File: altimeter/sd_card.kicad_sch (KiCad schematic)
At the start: 7 parts, among them J5 Micro_SD_Card

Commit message: add footprints to all components but e-match connectors
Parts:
- J5: footprint canhw:microSD_Molex_WM6698CT-ND -> canhw_footprints:microSD_Molex_WM6698CT-ND
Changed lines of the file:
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@@
 			)
 		)
-		(property "Footprint" "canhw:microSD_Molex_WM6698CT-ND"
+		(property "Footprint" "canhw_footprints:microSD_Molex_WM6698CT-ND"
 			(at 222.504 96.52 0)
 			(effects

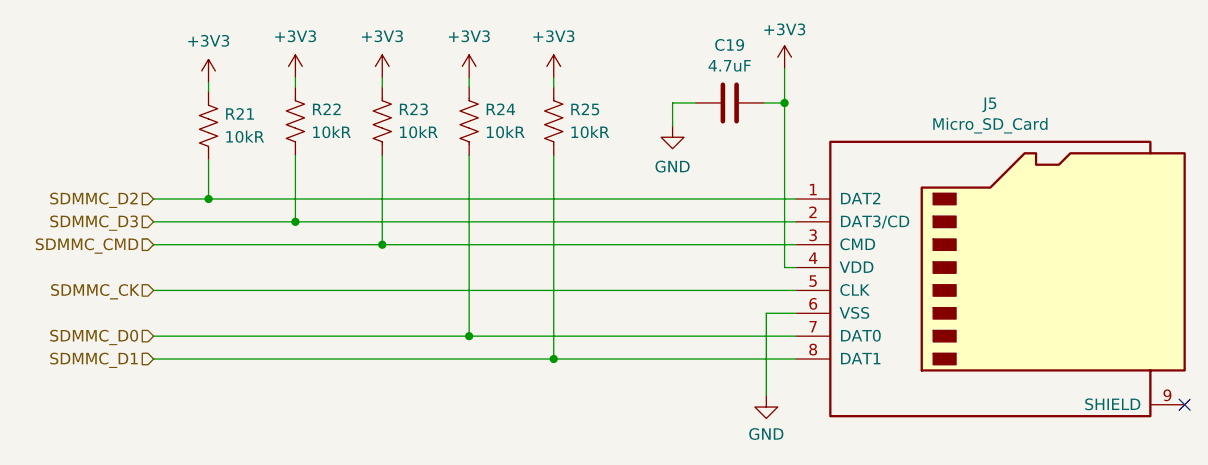
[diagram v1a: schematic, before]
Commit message: renumber all refdes
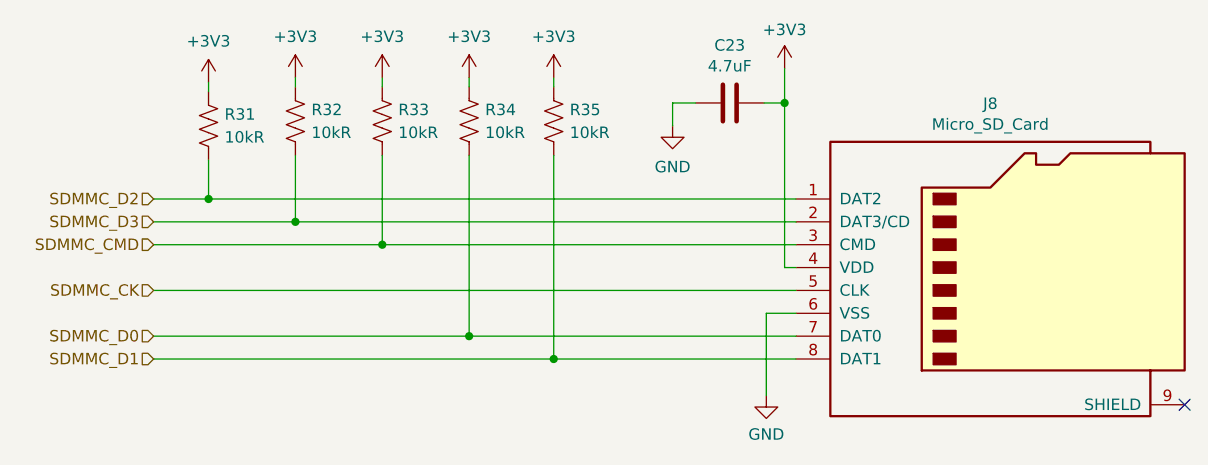
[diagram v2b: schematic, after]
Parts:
- renumbered C19 to C23, J5 to J8, R21 to R31, R22 to R32, R23 to R33, R24 to R34, R25 to R35
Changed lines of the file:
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@@
 		(dnp no)
 		(fields_autoplaced yes)
-		(property "Reference" "R23"
+		(property "Reference" "R33"
 			(at 126.238 86.614 0)
 			(effects
@@
 			(project "altimeter"
 				(path "/d279ec14-0cf9-4295-bb74-26f70799167d/bb0bce4a-66e8-4d50-ad75-3628c6e07bf2/e008a181-ebf7-4a64-a582-05387fd5f501"
-					(reference "R23")
+					(reference "R33")
 					(unit 1)
 				)
@@
 		(dnp no)
 		(fields_autoplaced yes)
-		(property "Reference" "#PWR050"
+		(property "Reference" "#PWR077"
 			(at 114.808 86.868 0)
 			(effects
@@
 			(project "altimeter"
 				(path "/d279ec14-0cf9-4295-bb74-26f70799167d/bb0bce4a-66e8-4d50-ad75-3628c6e07bf2/e008a181-ebf7-4a64-a582-05387fd5f501"
-					(reference "#PWR050")
+					(reference "#PWR077")
 					(unit 1)
 				)
@@
 		(dnp no)
 		(fields_autoplaced yes)
-		(property "Reference" "#PWR052"
+		(property "Reference" "#PWR079"
 			(at 134.112 86.868 0)
 			(effects
@@
 			(project "altimeter"
 				(path "/d279ec14-0cf9-4295-bb74-26f70799167d/bb0bce4a-66e8-4d50-ad75-3628c6e07bf2/e008a181-ebf7-4a64-a582-05387fd5f501"
-					(reference "#PWR052")
+					(reference "#PWR079")
 					(unit 1)
 				)
@@
 		(dnp no)
 		(fields_autoplaced yes)
-		(property "Reference" "#PWR051"
+		(property "Reference" "#PWR078"
 			(at 124.46 86.868 0)
 			(effects
@@
 			(project "altimeter"
 				(path "/d279ec14-0cf9-4295-bb74-26f70799167d/bb0bce4a-66e8-4d50-ad75-3628c6e07bf2/e008a181-ebf7-4a64-a582-05387fd5f501"
-					(reference "#PWR051")
+					(reference "#PWR078")
 					(unit 1)
 				)
@@
 		(dnp no)
 		(fields_autoplaced yes)
-		(property "Reference" "#PWR053"
+		(property "Reference" "#PWR080"
 			(at 143.51 86.868 0)
 			(effects
@@
 			(project "altimeter"
 				(path "/d279ec14-0cf9-4295-bb74-26f70799167d/bb0bce4a-66e8-4d50-ad75-3628c6e07bf2/e008a181-ebf7-4a64-a582-05387fd5f501"
-					(reference "#PWR053")
+					(reference "#PWR080")
 					(unit 1)
 				)
@@
 		(dnp no)
 		(fields_autoplaced yes)
-		(property "Reference" "R25"
+		(property "Reference" "R35"
 			(at 145.288 86.614 0)
 			(effects
@@
 			(project "altimeter"
 				(path "/d279ec14-0cf9-4295-bb74-26f70799167d/bb0bce4a-66e8-4d50-ad75-3628c6e07bf2/e008a181-ebf7-4a64-a582-05387fd5f501"
-					(reference "R25")
+					(reference "R35")
 					(unit 1)
 				)
@@
 		(on_board yes)
 		(dnp no)
-		(property "Reference" "C19"
+		(property "Reference" "C23"
 			(at 163.068 79.4512 90)
 			(effects
@@
 			(project "altimeter"
 				(path "/d279ec14-0cf9-4295-bb74-26f70799167d/bb0bce4a-66e8-4d50-ad75-3628c6e07bf2/e008a181-ebf7-4a64-a582-05387fd5f501"
-					(reference "C19")
+					(reference "C23")
 					(unit 1)
 				)
@@
 		(dnp no)
 		(fields_autoplaced yes)
-		(property "Reference" "#PWR049"
+		(property "Reference" "#PWR076"
 			(at 105.156 87.376 0)
 			(effects
@@
 			(project "altimeter"
 				(path "/d279ec14-0cf9-4295-bb74-26f70799167d/bb0bce4a-66e8-4d50-ad75-3628c6e07bf2/e008a181-ebf7-4a64-a582-05387fd5f501"
-					(reference "#PWR049")
+					(reference "#PWR076")
 					(unit 1)
 				)
@@
 		(dnp no)
 		(fields_autoplaced yes)
-		(property "Reference" "R21"
+		(property "Reference" "R31"
 			(at 106.934 87.122 0)
 			(effects
@@
 			(project "altimeter"
 				(path "/d279ec14-0cf9-4295-bb74-26f70799167d/bb0bce4a-66e8-4d50-ad75-3628c6e07bf2/e008a181-ebf7-4a64-a582-05387fd5f501"
-					(reference "R21")
+					(reference "R31")
 					(unit 1)
 				)
@@
 		(dnp no)
 		(fields_autoplaced yes)
-		(property "Reference" "R22"
+		(property "Reference" "R32"
 			(at 116.586 86.614 0)
 			(effects
@@
 			(project "altimeter"
 				(path "/d279ec14-0cf9-4295-bb74-26f70799167d/bb0bce4a-66e8-4d50-ad75-3628c6e07bf2/e008a181-ebf7-4a64-a582-05387fd5f501"
-					(reference "R22")
+					(reference "R32")
 					(unit 1)
 				)
@@
 		(dnp no)
 		(fields_autoplaced yes)
-		(property "Reference" "#PWR055"
+		(property "Reference" "#PWR082"
 			(at 167.132 124.714 0)
 			(effects
@@
 			(project "altimeter"
 				(path "/d279ec14-0cf9-4295-bb74-26f70799167d/bb0bce4a-66e8-4d50-ad75-3628c6e07bf2/e008a181-ebf7-4a64-a582-05387fd5f501"
-					(reference "#PWR055")
+					(reference "#PWR082")
 					(unit 1)
 				)
@@
 		(dnp no)
 		(fields_autoplaced yes)
-		(property "Reference" "#PWR056"
+		(property "Reference" "#PWR083"
 			(at 169.164 85.852 0)
 			(effects
@@
 			(project "altimeter"
 				(path "/d279ec14-0cf9-4295-bb74-26f70799167d/bb0bce4a-66e8-4d50-ad75-3628c6e07bf2/e008a181-ebf7-4a64-a582-05387fd5f501"
-					(reference "#PWR056")
+					(reference "#PWR083")
 					(unit 1)
 				)
@@
 		(dnp no)
 		(fields_autoplaced yes)
-		(property "Reference" "R24"
+		(property "Reference" "R34"
 			(at 135.89 86.614 0)
 			(effects
@@
 			(project "altimeter"
 				(path "/d279ec14-0cf9-4295-bb74-26f70799167d/bb0bce4a-66e8-4d50-ad75-3628c6e07bf2/e008a181-ebf7-4a64-a582-05387fd5f501"
-					(reference "R24")
+					(reference "R34")
 					(unit 1)
 				)
@@
 		(on_board yes)
 		(dnp no)
-		(property "Reference" "J5"
+		(property "Reference" "J8"
 			(at 192.024 85.9282 0)
 			(effects
@@
 			(project "altimeter"
 				(path "/d279ec14-0cf9-4295-bb74-26f70799167d/bb0bce4a-66e8-4d50-ad75-3628c6e07bf2/e008a181-ebf7-4a64-a582-05387fd5f501"
-					(reference "J5")
+					(reference "J8")
 					(unit 1)
 				)
@@
 		(dnp no)
 		(fields_autoplaced yes)
-		(property "Reference" "#PWR054"
+		(property "Reference" "#PWR081"
 			(at 156.718 94.742 0)
 			(effects
@@
 			(project "altimeter"
 				(path "/d279ec14-0cf9-4295-bb74-26f70799167d/bb0bce4a-66e8-4d50-ad75-3628c6e07bf2/e008a181-ebf7-4a64-a582-05387fd5f501"
-					(reference "#PWR054")
-					(unit 1)
-				)
+					(reference "#PWR081")
+					(unit 1)
+				)

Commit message: address buck current backdrive, add pyro current limiting resistors, mag switch and fuses, voltage sensing, battery charge current sensing
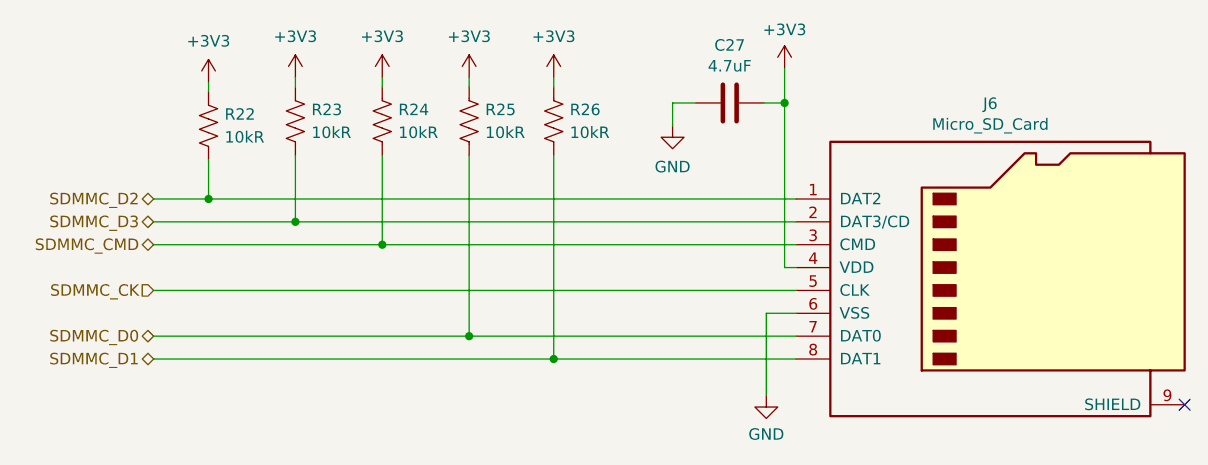
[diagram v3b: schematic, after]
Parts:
- renumbered C23 to C27, J8 to J6, R31 to R22, R32 to R23, R33 to R24, R34 to R25, R35 to R26
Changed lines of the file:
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@@
 	)
 	(hierarchical_label "SDMMC_D2"
-		(shape input)
+		(shape bidirectional)
 		(at 99.06 96.52 180)
 		(fields_autoplaced yes)
@@
 	)
 	(hierarchical_label "SDMMC_D0"
-		(shape input)
+		(shape bidirectional)
 		(at 99.06 111.76 180)
 		(fields_autoplaced yes)
@@
 	)
 	(hierarchical_label "SDMMC_D1"
-		(shape input)
+		(shape bidirectional)
 		(at 99.06 114.3 180)
 		(fields_autoplaced yes)
@@
 	)
 	(hierarchical_label "SDMMC_D3"
-		(shape input)
+		(shape bidirectional)
 		(at 99.06 99.06 180)
 		(fields_autoplaced yes)
@@
 	)
 	(hierarchical_label "SDMMC_CMD"
-		(shape input)
+		(shape bidirectional)
 		(at 99.06 101.6 180)
 		(fields_autoplaced yes)
@@
 		(dnp no)
 		(fields_autoplaced yes)
-		(property "Reference" "R33"
+		(property "Reference" "R24"
 			(at 126.238 86.614 0)
 			(effects
@@
 			(project "altimeter"
 				(path "/d279ec14-0cf9-4295-bb74-26f70799167d/bb0bce4a-66e8-4d50-ad75-3628c6e07bf2/e008a181-ebf7-4a64-a582-05387fd5f501"
-					(reference "R33")
+					(reference "R24")
 					(unit 1)
 				)
@@
 		(dnp no)
 		(fields_autoplaced yes)
-		(property "Reference" "#PWR077"
+		(property "Reference" "#PWR063"
 			(at 114.808 86.868 0)
 			(effects
@@
 			(project "altimeter"
 				(path "/d279ec14-0cf9-4295-bb74-26f70799167d/bb0bce4a-66e8-4d50-ad75-3628c6e07bf2/e008a181-ebf7-4a64-a582-05387fd5f501"
-					(reference "#PWR077")
+					(reference "#PWR063")
 					(unit 1)
 				)
@@
 		(dnp no)
 		(fields_autoplaced yes)
-		(property "Reference" "#PWR079"
+		(property "Reference" "#PWR065"
 			(at 134.112 86.868 0)
 			(effects
@@
 			(project "altimeter"
 				(path "/d279ec14-0cf9-4295-bb74-26f70799167d/bb0bce4a-66e8-4d50-ad75-3628c6e07bf2/e008a181-ebf7-4a64-a582-05387fd5f501"
-					(reference "#PWR079")
+					(reference "#PWR065")
 					(unit 1)
 				)
@@
 		(dnp no)
 		(fields_autoplaced yes)
-		(property "Reference" "#PWR078"
+		(property "Reference" "#PWR064"
 			(at 124.46 86.868 0)
 			(effects
@@
 			(project "altimeter"
 				(path "/d279ec14-0cf9-4295-bb74-26f70799167d/bb0bce4a-66e8-4d50-ad75-3628c6e07bf2/e008a181-ebf7-4a64-a582-05387fd5f501"
-					(reference "#PWR078")
+					(reference "#PWR064")
 					(unit 1)
 				)
@@
 		(dnp no)
 		(fields_autoplaced yes)
-		(property "Reference" "#PWR080"
+		(property "Reference" "#PWR066"
 			(at 143.51 86.868 0)
 			(effects
@@
 			(project "altimeter"
 				(path "/d279ec14-0cf9-4295-bb74-26f70799167d/bb0bce4a-66e8-4d50-ad75-3628c6e07bf2/e008a181-ebf7-4a64-a582-05387fd5f501"
-					(reference "#PWR080")
+					(reference "#PWR066")
 					(unit 1)
 				)
@@
 		(dnp no)
 		(fields_autoplaced yes)
-		(property "Reference" "R35"
+		(property "Reference" "R26"
 			(at 145.288 86.614 0)
 			(effects
@@
 			(project "altimeter"
 				(path "/d279ec14-0cf9-4295-bb74-26f70799167d/bb0bce4a-66e8-4d50-ad75-3628c6e07bf2/e008a181-ebf7-4a64-a582-05387fd5f501"
-					(reference "R35")
+					(reference "R26")
 					(unit 1)
 				)
@@
 		(on_board yes)
 		(dnp no)
-		(property "Reference" "C23"
+		(property "Reference" "C27"
 			(at 163.068 79.4512 90)
 			(effects
@@
 			(project "altimeter"
 				(path "/d279ec14-0cf9-4295-bb74-26f70799167d/bb0bce4a-66e8-4d50-ad75-3628c6e07bf2/e008a181-ebf7-4a64-a582-05387fd5f501"
-					(reference "C23")
+					(reference "C27")
 					(unit 1)
 				)
@@
 		(dnp no)
 		(fields_autoplaced yes)
-		(property "Reference" "#PWR076"
+		(property "Reference" "#PWR062"
 			(at 105.156 87.376 0)
 			(effects
@@
 			(project "altimeter"
 				(path "/d279ec14-0cf9-4295-bb74-26f70799167d/bb0bce4a-66e8-4d50-ad75-3628c6e07bf2/e008a181-ebf7-4a64-a582-05387fd5f501"
-					(reference "#PWR076")
+					(reference "#PWR062")
 					(unit 1)
 				)
@@
 		(dnp no)
 		(fields_autoplaced yes)
-		(property "Reference" "R31"
+		(property "Reference" "R22"
 			(at 106.934 87.122 0)
 			(effects
@@
 			(project "altimeter"
 				(path "/d279ec14-0cf9-4295-bb74-26f70799167d/bb0bce4a-66e8-4d50-ad75-3628c6e07bf2/e008a181-ebf7-4a64-a582-05387fd5f501"
-					(reference "R31")
+					(reference "R22")
 					(unit 1)
 				)
@@
 		(dnp no)
 		(fields_autoplaced yes)
-		(property "Reference" "R32"
+		(property "Reference" "R23"
 			(at 116.586 86.614 0)
 			(effects
@@
 			(project "altimeter"
 				(path "/d279ec14-0cf9-4295-bb74-26f70799167d/bb0bce4a-66e8-4d50-ad75-3628c6e07bf2/e008a181-ebf7-4a64-a582-05387fd5f501"
-					(reference "R32")
+					(reference "R23")
 					(unit 1)
 				)
@@
 		(dnp no)
 		(fields_autoplaced yes)
-		(property "Reference" "#PWR082"
+		(property "Reference" "#PWR068"
 			(at 167.132 124.714 0)
 			(effects
@@
 			(project "altimeter"
 				(path "/d279ec14-0cf9-4295-bb74-26f70799167d/bb0bce4a-66e8-4d50-ad75-3628c6e07bf2/e008a181-ebf7-4a64-a582-05387fd5f501"
-					(reference "#PWR082")
+					(reference "#PWR068")
 					(unit 1)
 				)
@@
 		(dnp no)
 		(fields_autoplaced yes)
-		(property "Reference" "#PWR083"
+		(property "Reference" "#PWR069"
 			(at 169.164 85.852 0)
 			(effects
@@
 			(project "altimeter"
 				(path "/d279ec14-0cf9-4295-bb74-26f70799167d/bb0bce4a-66e8-4d50-ad75-3628c6e07bf2/e008a181-ebf7-4a64-a582-05387fd5f501"
-					(reference "#PWR083")
+					(reference "#PWR069")
 					(unit 1)
 				)
@@
 		(dnp no)
 		(fields_autoplaced yes)
-		(property "Reference" "R34"
+		(property "Reference" "R25"
 			(at 135.89 86.614 0)
 			(effects
@@
 			(project "altimeter"
 				(path "/d279ec14-0cf9-4295-bb74-26f70799167d/bb0bce4a-66e8-4d50-ad75-3628c6e07bf2/e008a181-ebf7-4a64-a582-05387fd5f501"
-					(reference "R34")
+					(reference "R25")
 					(unit 1)
 				)
@@
 		(on_board yes)
 		(dnp no)
-		(property "Reference" "J8"
+		(property "Reference" "J6"
 			(at 192.024 85.9282 0)
 			(effects
@@
 			(project "altimeter"
 				(path "/d279ec14-0cf9-4295-bb74-26f70799167d/bb0bce4a-66e8-4d50-ad75-3628c6e07bf2/e008a181-ebf7-4a64-a582-05387fd5f501"
-					(reference "J8")
+					(reference "J6")
 					(unit 1)
 				)
@@
 		(dnp no)
 		(fields_autoplaced yes)
-		(property "Reference" "#PWR081"
+		(property "Reference" "#PWR067"
 			(at 156.718 94.742 0)
 			(effects
@@
 			(project "altimeter"
 				(path "/d279ec14-0cf9-4295-bb74-26f70799167d/bb0bce4a-66e8-4d50-ad75-3628c6e07bf2/e008a181-ebf7-4a64-a582-05387fd5f501"
-					(reference "#PWR081")
-					(unit 1)
-				)
+					(reference "#PWR067")
+					(unit 1)
+				)

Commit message: source/size buzzer, fuses, voltage divider resistors, add battery and +pyro voltage sense, gps connector and mcp2562, and capacitor to prevent brownout on 3v3
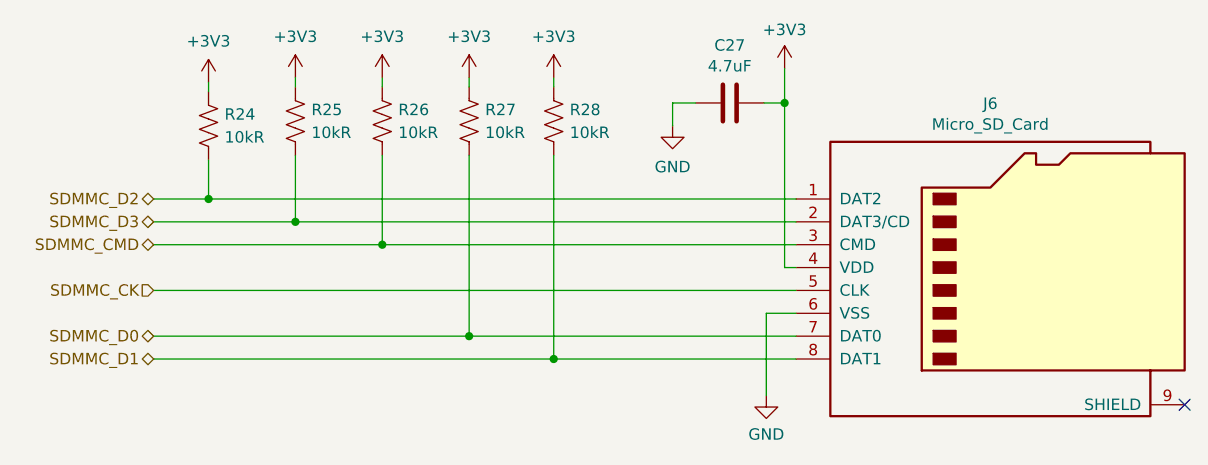
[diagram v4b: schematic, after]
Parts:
- renumbered R22 to R24, R23 to R25, R24 to R26, R25 to R27, R26 to R28
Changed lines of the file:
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@@
 		(dnp no)
 		(fields_autoplaced yes)
-		(property "Reference" "R24"
+		(property "Reference" "R26"
 			(at 126.238 86.614 0)
 			(effects
@@
 			(project "altimeter"
 				(path "/d279ec14-0cf9-4295-bb74-26f70799167d/bb0bce4a-66e8-4d50-ad75-3628c6e07bf2/e008a181-ebf7-4a64-a582-05387fd5f501"
-					(reference "R24")
+					(reference "R26")
 					(unit 1)
 				)
@@
 		(dnp no)
 		(fields_autoplaced yes)
-		(property "Reference" "#PWR063"
+		(property "Reference" "#PWR064"
 			(at 114.808 86.868 0)
 			(effects
@@
 			(project "altimeter"
 				(path "/d279ec14-0cf9-4295-bb74-26f70799167d/bb0bce4a-66e8-4d50-ad75-3628c6e07bf2/e008a181-ebf7-4a64-a582-05387fd5f501"
-					(reference "#PWR063")
+					(reference "#PWR064")
 					(unit 1)
 				)
@@
 		(dnp no)
 		(fields_autoplaced yes)
-		(property "Reference" "#PWR065"
+		(property "Reference" "#PWR066"
 			(at 134.112 86.868 0)
 			(effects
@@
 			(project "altimeter"
 				(path "/d279ec14-0cf9-4295-bb74-26f70799167d/bb0bce4a-66e8-4d50-ad75-3628c6e07bf2/e008a181-ebf7-4a64-a582-05387fd5f501"
-					(reference "#PWR065")
+					(reference "#PWR066")
 					(unit 1)
 				)
@@
 		(dnp no)
 		(fields_autoplaced yes)
-		(property "Reference" "#PWR064"
+		(property "Reference" "#PWR065"
 			(at 124.46 86.868 0)
 			(effects
@@
 			(project "altimeter"
 				(path "/d279ec14-0cf9-4295-bb74-26f70799167d/bb0bce4a-66e8-4d50-ad75-3628c6e07bf2/e008a181-ebf7-4a64-a582-05387fd5f501"
-					(reference "#PWR064")
+					(reference "#PWR065")
 					(unit 1)
 				)
@@
 		(dnp no)
 		(fields_autoplaced yes)
-		(property "Reference" "#PWR066"
+		(property "Reference" "#PWR067"
 			(at 143.51 86.868 0)
 			(effects
@@
 			(project "altimeter"
 				(path "/d279ec14-0cf9-4295-bb74-26f70799167d/bb0bce4a-66e8-4d50-ad75-3628c6e07bf2/e008a181-ebf7-4a64-a582-05387fd5f501"
-					(reference "#PWR066")
+					(reference "#PWR067")
 					(unit 1)
 				)
@@
 		(dnp no)
 		(fields_autoplaced yes)
-		(property "Reference" "R26"
+		(property "Reference" "R28"
 			(at 145.288 86.614 0)
 			(effects
@@
 			(project "altimeter"
 				(path "/d279ec14-0cf9-4295-bb74-26f70799167d/bb0bce4a-66e8-4d50-ad75-3628c6e07bf2/e008a181-ebf7-4a64-a582-05387fd5f501"
-					(reference "R26")
+					(reference "R28")
 					(unit 1)
 				)
@@
 		(dnp no)
 		(fields_autoplaced yes)
-		(property "Reference" "#PWR062"
+		(property "Reference" "#PWR063"
 			(at 105.156 87.376 0)
 			(effects
@@
 			(project "altimeter"
 				(path "/d279ec14-0cf9-4295-bb74-26f70799167d/bb0bce4a-66e8-4d50-ad75-3628c6e07bf2/e008a181-ebf7-4a64-a582-05387fd5f501"
-					(reference "#PWR062")
+					(reference "#PWR063")
 					(unit 1)
 				)
@@
 		(dnp no)
 		(fields_autoplaced yes)
-		(property "Reference" "R22"
+		(property "Reference" "R24"
 			(at 106.934 87.122 0)
 			(effects
@@
 			(project "altimeter"
 				(path "/d279ec14-0cf9-4295-bb74-26f70799167d/bb0bce4a-66e8-4d50-ad75-3628c6e07bf2/e008a181-ebf7-4a64-a582-05387fd5f501"
-					(reference "R22")
+					(reference "R24")
 					(unit 1)
 				)
@@
 		(dnp no)
 		(fields_autoplaced yes)
-		(property "Reference" "R23"
+		(property "Reference" "R25"
 			(at 116.586 86.614 0)
 			(effects
@@
 			(project "altimeter"
 				(path "/d279ec14-0cf9-4295-bb74-26f70799167d/bb0bce4a-66e8-4d50-ad75-3628c6e07bf2/e008a181-ebf7-4a64-a582-05387fd5f501"
-					(reference "R23")
+					(reference "R25")
 					(unit 1)
 				)
@@
 		(dnp no)
 		(fields_autoplaced yes)
-		(property "Reference" "#PWR068"
+		(property "Reference" "#PWR069"
 			(at 167.132 124.714 0)
 			(effects
@@
 			(project "altimeter"
 				(path "/d279ec14-0cf9-4295-bb74-26f70799167d/bb0bce4a-66e8-4d50-ad75-3628c6e07bf2/e008a181-ebf7-4a64-a582-05387fd5f501"
-					(reference "#PWR068")
+					(reference "#PWR069")
 					(unit 1)
 				)
@@
 		(dnp no)
 		(fields_autoplaced yes)
-		(property "Reference" "#PWR069"
+		(property "Reference" "#PWR070"
 			(at 169.164 85.852 0)
 			(effects
@@
 			(project "altimeter"
 				(path "/d279ec14-0cf9-4295-bb74-26f70799167d/bb0bce4a-66e8-4d50-ad75-3628c6e07bf2/e008a181-ebf7-4a64-a582-05387fd5f501"
-					(reference "#PWR069")
+					(reference "#PWR070")
 					(unit 1)
 				)
@@
 		(dnp no)
 		(fields_autoplaced yes)
-		(property "Reference" "R25"
+		(property "Reference" "R27"
 			(at 135.89 86.614 0)
 			(effects
@@
 			(project "altimeter"
 				(path "/d279ec14-0cf9-4295-bb74-26f70799167d/bb0bce4a-66e8-4d50-ad75-3628c6e07bf2/e008a181-ebf7-4a64-a582-05387fd5f501"
-					(reference "R25")
+					(reference "R27")
 					(unit 1)
 				)
@@
 		(dnp no)
 		(fields_autoplaced yes)
-		(property "Reference" "#PWR067"
+		(property "Reference" "#PWR068"
 			(at 156.718 94.742 0)
 			(effects
@@
 			(project "altimeter"
 				(path "/d279ec14-0cf9-4295-bb74-26f70799167d/bb0bce4a-66e8-4d50-ad75-3628c6e07bf2/e008a181-ebf7-4a64-a582-05387fd5f501"
-					(reference "#PWR067")
-					(unit 1)
-				)
+					(reference "#PWR068")
+					(unit 1)
+				)
